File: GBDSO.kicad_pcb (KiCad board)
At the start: 2 copper layers, 66 parts, among them P1 100k, P2 100k, U1 TL062, U2 DS1267_SOIC, U3 TL062, U4 MAX114CAG, U5 74HC175D, U6 74HC138D, U7 AT27C256R, U8 TLC272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

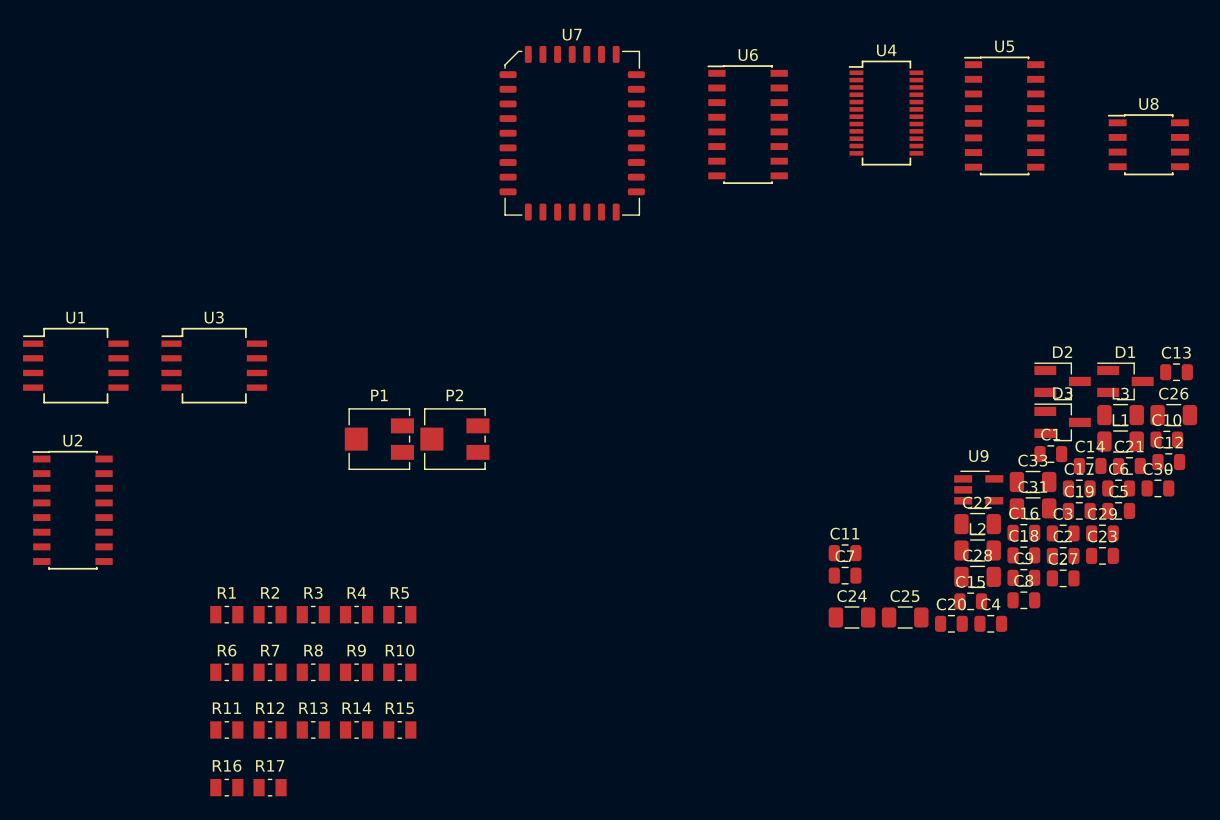
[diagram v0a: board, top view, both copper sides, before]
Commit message: updated pcb with new and all footprints
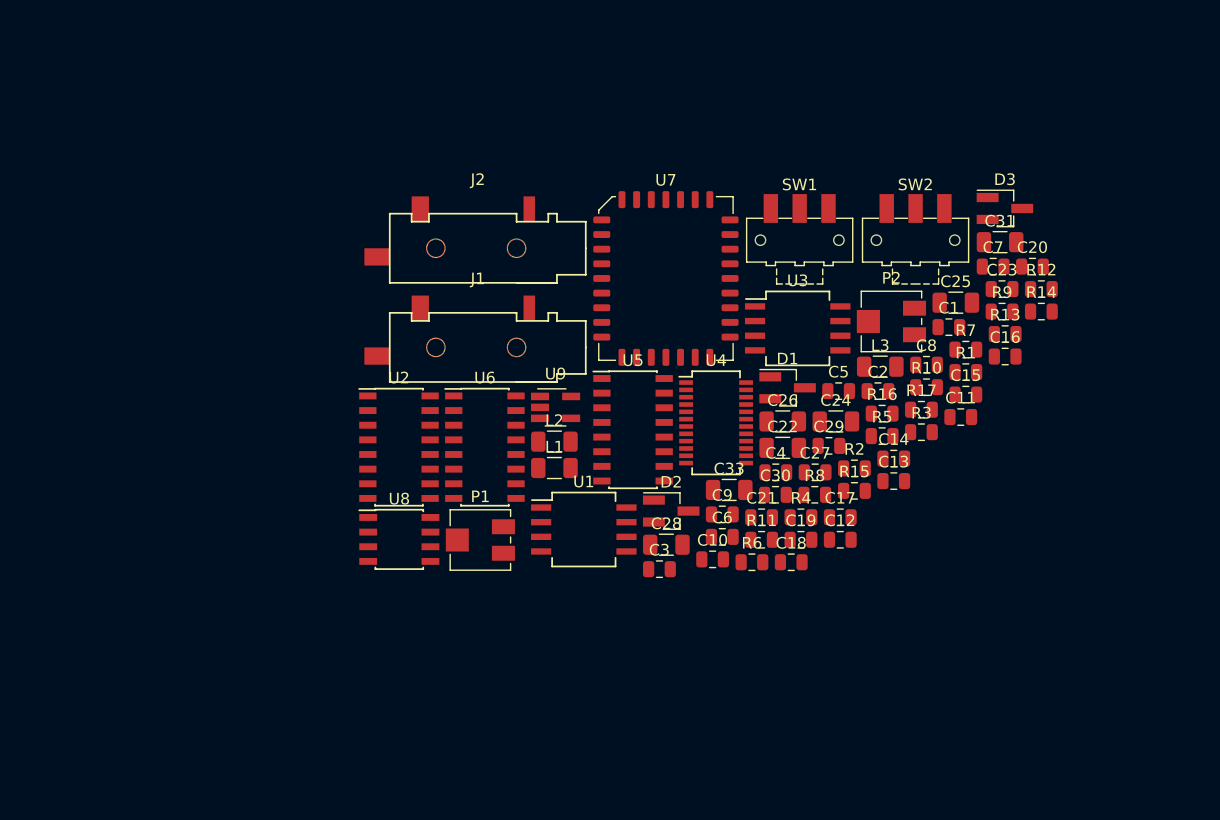
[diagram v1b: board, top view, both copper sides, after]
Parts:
- added J1: MJ-3523-SMT-TR, MJ-3523-SMT-TR:MJ-3523-SMT-TR, F.Cu at (170.6, 90.3)
- added J2: MJ-3523-SMT-TR, MJ-3523-SMT-TR:MJ-3523-SMT-TR, F.Cu at (170.6, 81.7)
- added SW1: SW_SPDT, Button_Switch_SMD:SW_SPDT_CK-JS102011SAQN, F.Cu at (198.5, 81.0)
- added SW2: SW_SPDT, Button_Switch_SMD:SW_SPDT_CK-JS102011SAQN, F.Cu at (208.5, 81.0)
- moved R12 77.0 mm to (219.4, 85.3)
- moved U8 73.5 mm to (163.8, 107.0)
- moved R14 69.6 mm to (219.4, 87.2)
- moved R13 69.1 mm to (216.3, 89.2)
- moved R1 67.5 mm to (212.9, 92.5)
- moved R7 66.5 mm to (212.9, 90.5)
- moved R16 65.4 mm to (205.6, 96.1)
- moved R17 65.3 mm to (209.0, 95.7)
- moved R9 64.1 mm to (216.0, 87.2)
- moved R3 55.1 mm to (209.0, 97.7)
- moved R2 52.2 mm to (203.2, 100.8)
- moved R10 51.9 mm to (209.5, 93.8)
- moved U3 50.7 mm to (198.3, 88.7)
- moved R11 49.2 mm to (195.2, 107.0)
- moved L1 49.2 mm to (177.2, 100.8)
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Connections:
- net Net-(U6-Pad2) renamed /~WR
- net Net-(U6-Pad5) renamed /ECLK
- net Net-(U7-Pad10) renamed /A1
- net Net-(U7-Pad11) renamed /A0
- net Net-(U7-Pad24) renamed /A10
- net Net-(U7-Pad27) renamed /A11
- net Net-(U7-Pad28) renamed /A9
- net Net-(U7-Pad29) renamed /A8
- net Net-(U7-Pad3) renamed /A12
- net Net-(U7-Pad4) renamed /A7
- net Net-(U7-Pad5) renamed /A6
- net Net-(U7-Pad6) renamed /A5
- net Net-(U7-Pad7) renamed /A4
- net Net-(U7-Pad8) renamed /A3
- net Net-(U7-Pad9) renamed /A2
- C18 pad 1: Net-(C18-Pad1) -> +5V
- C18 pad 2: Net-(C18-Pad2) -> GND
- C22 pad 1: Net-(C22-Pad1) -> +5V
- C22 pad 2: Net-(C22-Pad2) -> GND
- C23 pad 1: Net-(C23-Pad1) -> +5V
- C23 pad 2: Net-(C23-Pad2) -> GND
- C25 pad 2: Net-(C25-Pad2) -> GND
- C26 pad 1: Net-(C26-Pad1) -> -5V
- C26 pad 2: Net-(C26-Pad2) -> GND
- C27 pad 1: Net-(C27-Pad1) -> -5V
- C27 pad 2: Net-(C27-Pad2) -> GND
- C28 pad 1: Net-(C28-Pad1) -> +5V
- C28 pad 2: Net-(C28-Pad2) -> GND
- C29 pad 1: Net-(C29-Pad1) -> +5V
- C29 pad 2: Net-(C29-Pad2) -> GND
- C30 pad 1: Net-(C30-Pad1) -> +5V
- C30 pad 2: Net-(C30-Pad2) -> GND
- C31 pad 1: Net-(C31-Pad1) -> +5VA
- C31 pad 2: Net-(C31-Pad2) -> GND
- C33 pad 1: Net-(C33-Pad1) -> +5VC
- C33 pad 2: Net-(C33-Pad2) -> GND
- L1 pad 1: Net-(L1-Pad1) -> Net-(C25-Pad1)
- L1 pad 2: Net-(L1-Pad2) -> -5V
- L2 pad 1: Net-(L2-Pad1) -> +5V
- L2 pad 2: Net-(L2-Pad2) -> +5VA
- L3 pad 1: Net-(L3-Pad1) -> +5V
- L3 pad 2: Net-(L3-Pad2) -> +5VC
- U4 pad 12: Net-(U4-Pad12) -> GND
- U4 pad 17: Net-(U4-Pad17) -> /D4
- U4 pad 18: Net-(U4-Pad18) -> /D5
- U4 pad 19: Net-(U4-Pad19) -> /D6
- U4 pad 20: Net-(U4-Pad20) -> /D7
- U4 pad 6: Net-(U4-Pad6) -> /D0
- U4 pad 7: Net-(U4-Pad7) -> /D1
- U4 pad 8: Net-(U4-Pad8) -> /D2
- U4 pad 9: Net-(U4-Pad9) -> /D3
- U5 pad 12: Net-(U5-Pad12) -> /D7
- U5 pad 13: Net-(U5-Pad13) -> /D4
- U5 pad 16: Net-(U5-Pad16) -> +5V
- U5 pad 4: Net-(U5-Pad4) -> /D5
- U5 pad 5: Net-(U5-Pad5) -> /D6
- U5 pad 8: Net-(U5-Pad8) -> GND
- U6 pad 1: Net-(U6-Pad1) -> /~RD
- U6 pad 16: Net-(U6-Pad16) -> +5V
- U6 pad 3: Net-(U6-Pad3) -> /A13
- U6 pad 4: Net-(U6-Pad4) -> /A15
- U6 pad 6: Net-(U6-Pad6) -> /A14
- U6 pad 8: Net-(U6-Pad8) -> GND
- U7 pad 13: Net-(U7-Pad13) -> /D0
- U7 pad 14: Net-(U7-Pad14) -> /D1
- U7 pad 15: Net-(U7-Pad15) -> /D2
- U7 pad 16: Net-(U7-Pad16) -> GND
- U7 pad 18: Net-(U7-Pad18) -> /D3
- U7 pad 19: Net-(U7-Pad19) -> /D4
- U7 pad 2: Net-(U7-Pad2) -> +5V
- U7 pad 20: Net-(U7-Pad20) -> /D5
- U7 pad 21: Net-(U7-Pad21) -> /D6
- U7 pad 22: Net-(U7-Pad22) -> /D7
- U7 pad 23: Net-(U7-Pad23) -> /A15
- U7 pad 25: Net-(U7-Pad25) -> /~RD
- U7 pad 30: Net-(U7-Pad30) -> /A13
- U7 pad 31: Net-(U7-Pad31) -> /A14
- U7 pad 32: Net-(U7-Pad32) -> +5V
- U9 pad 1: Net-(U9-Pad1) -> Net-(C25-Pad1)
- U9 pad 2: Net-(U9-Pad2) -> +5V
- U9 pad 3: Net-(U9-Pad3) -> Net-(C24-Pad2)
- U9 pad 4: Net-(U9-Pad4) -> GND
- U9 pad 5: Net-(U9-Pad5) -> Net-(C24-Pad1)

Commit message: updated pcb
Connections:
- C1 pad 2: Net-(C1-Pad2) -> GND
- C10 pad 2: Net-(C10-Pad2) -> GND
- C11 pad 2: Net-(C11-Pad2) -> Net-(C10-Pad1)
- C12 pad 1: Net-(C12-Pad1) -> GND
- C12 pad 2: Net-(C12-Pad2) -> -5V
- C14 pad 1: Net-(C14-Pad1) -> +5VA
- C14 pad 2: Net-(C14-Pad2) -> GND
- C16 pad 2: Net-(C16-Pad2) -> GND
- C17 pad 1: Net-(C17-Pad1) -> +5VC
- C17 pad 2: Net-(C17-Pad2) -> GND
- C19 pad 2: Net-(C19-Pad2) -> GND
- C2 pad 1: Net-(C2-Pad1) -> Net-(C1-Pad1)
- C20 pad 1: Net-(C20-Pad1) -> +5VA
- C20 pad 2: Net-(C20-Pad2) -> GND
- C21 pad 1: Net-(C21-Pad1) -> -5V
- C21 pad 2: Net-(C21-Pad2) -> GND
- C4 pad 1: Net-(C4-Pad1) -> GND
- C4 pad 2: Net-(C4-Pad2) -> -5V
- C5 pad 1: Net-(C5-Pad1) -> +5VA
- C5 pad 2: Net-(C5-Pad2) -> GND
- C7 pad 2: Net-(C7-Pad2) -> GND
- C8 pad 2: Net-(C8-Pad2) -> -5V
- C9 pad 1: Net-(C9-Pad1) -> +5VA
- C9 pad 2: Net-(C9-Pad2) -> GND
- D1 pad 1: Net-(D1-Pad1) -> -5V
- D1 pad 2: Net-(D1-Pad2) -> +5V
- D1 pad 3: Net-(D1-Pad3) -> Net-(C3-Pad1)
- D2 pad 1: Net-(D2-Pad1) -> -5V
- D2 pad 2: Net-(D2-Pad2) -> +5V
- D2 pad 3: Net-(D2-Pad3) -> Net-(C13-Pad1)
- D3 pad 1: Net-(D3-Pad1) -> Net-(C19-Pad1)
- D3 pad 2: Net-(D3-Pad2) -> GND
- J1 pad 1: Net-(J1-Pad1) -> GND
- J1 pad 2: Net-(J1-Pad2) -> Net-(C1-Pad1)
- J2 pad 1: Net-(J2-Pad1) -> GND
- J2 pad 2: Net-(J2-Pad2) -> Net-(C10-Pad1)
- P1 pad 1: Net-(P1-Pad1) -> -2.5V
- P1 pad 3: Net-(P1-Pad3) -> +2.5V
- P2 pad 1: Net-(P2-Pad1) -> -2.5V
- P2 pad 3: Net-(P2-Pad3) -> +2.5V
- R1 pad 1: Net-(R1-Pad1) -> Net-(C3-Pad1)
- R1 pad 2: Net-(R1-Pad2) -> Net-(C2-Pad2)
- R10 pad 1: Net-(R10-Pad1) -> Net-(P2-Pad2)
- R11 pad 1: Net-(R11-Pad1) -> GND
- R11 pad 2: Net-(R11-Pad2) -> Net-(R10-Pad2)
- R12 pad 1: Net-(R12-Pad1) -> Net-(C13-Pad2)
- R12 pad 2: Net-(R12-Pad2) -> Net-(C13-Pad1)
- R13 pad 1: Net-(R13-Pad1) -> Net-(C16-Pad1)
- R13 pad 2: Net-(R13-Pad2) -> Net-(C15-Pad1)
- R14 pad 1: Net-(R14-Pad1) -> Net-(C16-Pad1)
- R14 pad 2: Net-(R14-Pad2) -> +2.5V
- R15 pad 1: Net-(R15-Pad1) -> Net-(C19-Pad1)
- R15 pad 2: Net-(R15-Pad2) -> +5VA
- R16 pad 2: Net-(R16-Pad2) -> +2.5V
- R17 pad 1: Net-(R17-Pad1) -> -2.5V
- R17 pad 2: Net-(R17-Pad2) -> Net-(R16-Pad1)
- R2 pad 2: Net-(R2-Pad2) -> Net-(C3-Pad1)
- R3 pad 1: Net-(R3-Pad1) -> Net-(P1-Pad2)
- R3 pad 2: Net-(R3-Pad2) -> Net-(R2-Pad1)
- R4 pad 1: Net-(R4-Pad1) -> GND
- R4 pad 2: Net-(R4-Pad2) -> Net-(R2-Pad1)
- R5 pad 1: Net-(R5-Pad1) -> Net-(C3-Pad2)
- R5 pad 2: Net-(R5-Pad2) -> Net-(C3-Pad1)
- R6 pad 1: Net-(R6-Pad1) -> Net-(C7-Pad1)
- R6 pad 2: Net-(R6-Pad2) -> Net-(C6-Pad2)
- R7 pad 1: Net-(R7-Pad1) -> Net-(C7-Pad1)
- R7 pad 2: Net-(R7-Pad2) -> +2.5V
- R8 pad 1: Net-(R8-Pad1) -> Net-(C13-Pad1)
- R8 pad 2: Net-(R8-Pad2) -> Net-(C11-Pad1)
- R9 pad 2: Net-(R9-Pad2) -> Net-(C13-Pad1)
- SW1 pad 1: Net-(SW1-Pad1) -> Net-(C1-Pad1)
- SW1 pad 2: Net-(SW1-Pad2) -> Net-(C2-Pad2)
- SW2 pad 1: Net-(SW2-Pad1) -> Net-(C10-Pad1)
- SW2 pad 2: Net-(SW2-Pad2) -> Net-(C11-Pad1)
- U1 pad 1: Net-(U1-Pad1) -> Net-(C6-Pad2)
- U1 pad 2: Net-(U1-Pad2) -> Net-(C6-Pad1)
- U1 pad 3: Net-(U1-Pad3) -> GND
- U1 pad 5: Net-(U1-Pad5) -> GND
- U1 pad 6: Net-(U1-Pad6) -> Net-(C3-Pad1)
- U1 pad 7: Net-(U1-Pad7) -> Net-(C3-Pad2)
- U1 pad 8: Net-(U1-Pad8) -> -5V
- U2 pad 1: Net-(U2-Pad1) -> Net-(C8-Pad1)
- U2 pad 11: Net-(U2-Pad11) -> Net-(C6-Pad2)
- U2 pad 12: Net-(U2-Pad12) -> Net-(C6-Pad1)
- U2 pad 13: Net-(U2-Pad13) -> Net-(C3-Pad2)
- U2 pad 16: Net-(U2-Pad16) -> +5VA
- U2 pad 3: Net-(U2-Pad3) -> Net-(C13-Pad2)
- U2 pad 4: Net-(U2-Pad4) -> Net-(C15-Pad1)
- U2 pad 5: Net-(U2-Pad5) -> Net-(C15-Pad2)
- U2 pad 8: Net-(U2-Pad8) -> GND
- U2 pad 9: Net-(U2-Pad9) -> /D1
- U3 pad 1: Net-(U3-Pad1) -> Net-(C13-Pad2)
- U3 pad 2: Net-(U3-Pad2) -> Net-(C13-Pad1)
- U3 pad 3: Net-(U3-Pad3) -> GND
- U3 pad 5: Net-(U3-Pad5) -> GND
- U3 pad 6: Net-(U3-Pad6) -> Net-(C15-Pad2)
- U3 pad 7: Net-(U3-Pad7) -> Net-(C15-Pad1)
- U3 pad 8: Net-(U3-Pad8) -> -5V
- U4 pad 1: Net-(U4-Pad1) -> GND
- U4 pad 13: Net-(U4-Pad13) -> GND
- U4 pad 14: Net-(U4-Pad14) -> +2.5V
- U4 pad 15: Net-(U4-Pad15) -> Net-(U4-Pad10)
- U4 pad 16: Net-(U4-Pad16) -> Net-(U4-Pad10)
- U4 pad 2: Net-(U4-Pad2) -> GND
- U4 pad 21: Net-(U4-Pad21) -> GND
- U4 pad 24: Net-(U4-Pad24) -> +5VC
- U4 pad 3: Net-(U4-Pad3) -> Net-(C7-Pad1)
- U4 pad 4: Net-(U4-Pad4) -> Net-(C16-Pad1)
- U4 pad 5: Net-(U4-Pad5) -> +5VC
- U5 pad 1: Net-(U5-Pad1) -> +5V
- U5 pad 10: Net-(U5-Pad10) -> Net-(U4-Pad22)
- U5 pad 15: Net-(U5-Pad15) -> Net-(U2-Pad7)
- U5 pad 2: Net-(U5-Pad2) -> Net-(U2-Pad6)
- U5 pad 7: Net-(U5-Pad7) -> Net-(U4-Pad23)
- U6 pad 10: Net-(U6-Pad10) -> Net-(U5-Pad9)
- U6 pad 9: Net-(U6-Pad9) -> Net-(U4-Pad10)
- U8 pad 1: Net-(U8-Pad1) -> +2.5V
- U8 pad 2: Net-(U8-Pad2) -> +2.5V
- U8 pad 3: Net-(U8-Pad3) -> Net-(C19-Pad1)
- U8 pad 4: Net-(U8-Pad4) -> -5V
- U8 pad 5: Net-(U8-Pad5) -> GND
- U8 pad 6: Net-(U8-Pad6) -> Net-(R16-Pad1)
- U8 pad 7: Net-(U8-Pad7) -> -2.5V
- U8 pad 8: Net-(U8-Pad8) -> +5VA

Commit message: updated PCB
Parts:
- moved L3 253.5 mm to (-27.4, -8.14)
- moved R16 252.0 mm to (-27.4, -0.06)
- moved R17 250.2 mm to (-19.4, -6.41)
- moved C30 241.3 mm to (-24.0, 4.89)
- moved C4 234.1 mm to (-17.5, 6.03)
- moved C21 228.5 mm to (-15.6, 16.8)
- moved C14 228.0 mm to (-0.52, 4.64)
- moved C33 226.7 mm to (-15.0, 11.0)
- moved C5 226.5 mm to (-3.81, -0.83)
- moved C28 226.3 mm to (-22.7, 22.0)
- moved C31 224.0 mm to (11.1, -9.53)
- moved C29 223.9 mm to (-4.64, 10.2)
- moved C20 220.6 mm to (18.2, -8.83)
- moved L2 219.2 mm to (-24.2, 11.9)
- moved C3 219.2 mm to (-15.0, 23.0)
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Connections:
- R9 pad 1: Net-(R9-Pad1) -> Net-(R10-Pad2)
- U1 pad 4: Net-(U1-Pad4) -> -5V
- U1 pad 8: -5V -> +5VA
- U3 pad 1: Net-(C13-Pad2) -> Net-(C15-Pad1)
- U3 pad 2: Net-(C13-Pad1) -> Net-(C15-Pad2)
- U3 pad 4: Net-(U3-Pad4) -> -5V
- U3 pad 6: Net-(C15-Pad2) -> Net-(C13-Pad1)
- U3 pad 7: Net-(C15-Pad1) -> Net-(C13-Pad2)
- U3 pad 8: -5V -> +5VA
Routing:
- net GND: track 0.00 -> 41.3 mm
- net Net-(C3-Pad1): track 0.00 -> 14.4 mm
- net Net-(C13-Pad1): track 0.00 -> 14.4 mm
- net -5V: track 0.00 -> 13.9 mm
- net Net-(C15-Pad1): track 0.00 -> 10.5 mm
- net Net-(C6-Pad2): track 0.00 -> 10.4 mm
- net +5V: track 0.00 -> 8.13 mm
- net Net-(C24-Pad2): track 0.00 -> 6.59 mm
- net Net-(C3-Pad2): track 0.00 -> 5.32 mm
- net Net-(C13-Pad2): track 0.00 -> 5.11 mm
- net Net-(C16-Pad1): track 0.00 -> 4.95 mm
- net Net-(R10-Pad2): track 0.00 -> 4.87 mm
- net Net-(C7-Pad1): track 0.00 -> 4.85 mm
- net Net-(R2-Pad1): track 0.00 -> 4.84 mm
- net Net-(C25-Pad1): track 0.00 -> 4.79 mm
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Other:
- board outline added: 51 x 61 mm
- rule trace_min: 0.2 -> 0.12
- board text added: "Edge connector"

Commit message: updated PCB, changed track width, started with routing power and GND. Also, bottom layer is a GND plane
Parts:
- moved C18 207.2 mm to (83.3, 133.5), turned to 270 degrees
- moved L3 204.0 mm to (124.2, 128.3)
- moved R16 195.2 mm to (115.4, 133.1), turned to 180 degrees
- moved R17 194.6 mm to (118.2, 131.2), turned to 270 degrees
- moved L2 185.0 mm to (122.8, 124.3), turned to 180 degrees
- moved C33 183.2 mm to (127.8, 125.9), turned to 180 degrees
- moved C19 182.7 mm to (104.9, 125.6), turned to 90 degrees
- moved C13 174.1 mm to (106.3, 96.9), turned to 180 degrees
- moved C21 172.5 mm to (111.8, 133.1)
- moved C31 170.6 mm to (118.2, 123.2), turned to 90 degrees
- moved C4 170.3 mm to (116.8, 110.9), turned to 270 degrees
- moved C20 169.0 mm to (119.0, 126.9)
- moved C17 167.8 mm to (128.3, 130.1), turned to 180 degrees
- moved C16 167.6 mm to (113.1, 137.2), turned to 0 degrees
- moved D2 162.3 mm to (97.0, 111.8), turned to 0 degrees
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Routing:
- net +5V: track 8.13 -> 103.4 mm
- net GND: track 41.3 -> 68.1 mm, vias 0 -> 29
- net Net-(C1-Pad1): track 4.32 -> 25.8 mm
- net Net-(C10-Pad1): track 4.28 -> 24.5 mm
- net +5VA: track 2.01 -> 16.7 mm
- net Net-(C11-Pad1): track 1.62 -> 14.4 mm
- net +5VC: track 0.00 -> 12.5 mm
- net -5V: track 13.9 -> 26.1 mm
- net Net-(C2-Pad2): track 1.65 -> 11.5 mm
- net Net-(P2-Pad2): track 0.00 -> 8.11 mm
- net Net-(C15-Pad2): track 3.71 -> 11.7 mm
- net Net-(C13-Pad2): track 5.11 -> 12.6 mm
- net Net-(C25-Pad1): track 4.79 -> 11.7 mm
- net +2.5V: track 0.00 -> 6.65 mm
- net Net-(U4-Pad10): track 0.00 -> 5.83 mm
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- added copper zone on B.Cu, net GND
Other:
- outline, holes or cut-outs redrawn

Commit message: updated schematic, new generated netlist, finished pcb
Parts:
- added J3: GB_EdgeConnector, GB_EdgeConnector:GB_EdgeConnector, F.Cu at (105.5, 148.1)
- added REF**: KiCad-Logo_6mm_SilkScreen, Symbol:KiCad-Logo_6mm_SilkScreen, B.Cu at (122.2, 148.0)
- added REF**: OSHW-Symbol_6.7x6mm_SilkScreen, Symbol:OSHW-Symbol_6.7x6mm_SilkScreen, B.Cu at (86.0, 148.2)
- moved D3 1.11 mm to (106.3, 129.1), turned to 0 degrees
- moved R2 0.58 mm to (123.2, 103.6)
- moved C6 0.49 mm to (119.5, 103.5)
- moved R5 0.42 mm to (123.3, 101.4)
- moved C3 0.32 mm to (123.3, 99.2)
- moved C9 0.29 mm to (119.5, 101.4)
- moved C4 0.23 mm to (116.8, 110.7)
- moved C5 0.09 mm to (119.5, 99.2)
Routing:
- net +2.5V: track 6.65 -> 114.0 mm, vias 0 -> 7
- net /D1: track 0.00 -> 82.4 mm, vias 0 -> 4
- net /D5: track 0.00 -> 74.6 mm, vias 0 -> 4
- net -2.5V: track 0.00 -> 74.4 mm, vias 0 -> 3
- net /D4: track 0.00 -> 72.1 mm, vias 0 -> 2
- net /D6: track 0.00 -> 70.7 mm, vias 0 -> 2
- net +5VA: track 16.7 -> 87.0 mm, vias 0 -> 2
- net /D7: track 0.00 -> 64.1 mm, vias 0 -> 2
- net /A15: track 0.00 -> 62.9 mm, vias 0 -> 2
- net /A13: track 0.00 -> 54.8 mm, vias 0 -> 2
- net -5V: track 26.1 -> 80.5 mm, vias 0 -> 5
- net /D3: track 0.00 -> 54.2 mm, vias 0 -> 2
- net Net-(U4-Pad23): track 0.00 -> 53.9 mm, vias 0 -> 2
- net +5V: track 103.4 -> 154.9 mm, vias 0 -> 2
- net /A14: track 0.00 -> 51.2 mm, vias 0 -> 2
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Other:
- outline, holes or cut-outs redrawn
- board text added: "GBDSO by Steve Willis (2000/10)"
- board text added: "github.com/pyroesp/GBDSO"
- board text removed: "Edge connector"

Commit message: final update of pcb, updated images
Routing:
- net /A8: track 34.3 -> 30.6 mm
- net /A9: track 38.5 -> 35.0 mm
- net /A10: track 42.2 -> 38.8 mm
- net /A11: track 39.7 -> 36.3 mm
- net /A13: track 54.8 -> 51.6 mm
- net /A14: track 51.2 -> 48.3 mm
- net /D3: track 54.2 -> 51.9 mm
- net /D4: track 72.1 -> 69.9 mm
- net /D5: track 74.6 -> 73.0 mm
- net Net-(U4-Pad10): track 56.0 -> 54.5 mm
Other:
- outline, holes or cut-outs redrawn

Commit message: general update and lib fix + new generated gerber
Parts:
- J3: value GB_EdgeConnector -> Conn_01x32
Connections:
- U2 pad 15: Net-(U2-Pad15) -> (no net)
- U2 pad 2: Net-(U2-Pad2) -> (no net)
